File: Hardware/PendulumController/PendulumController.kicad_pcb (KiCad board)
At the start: 2 copper layers, 157 x 47 mm, 73 parts, among them J101 MOTOR, J102 ENCODER, J201 ICSP, J302 19V Input, J401 USBC, J402 PROG, Q101 MMBT3904, Q102 MMBT3906, SW201 RESET, SW202 START_SW, SW203 STOP/MODE_SW, U201 ATmega328P, U301 NCV1117ST50T3G, U401 FT232RL, Y201 16mHz

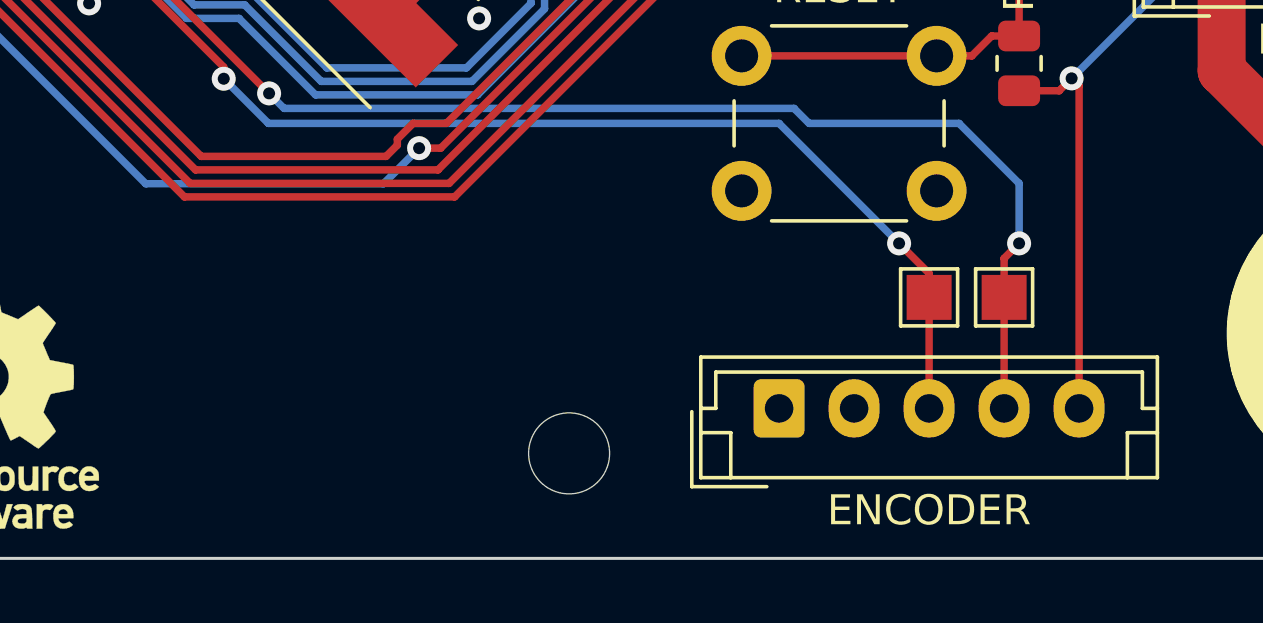
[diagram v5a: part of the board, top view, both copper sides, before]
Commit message: Add limit siwtch
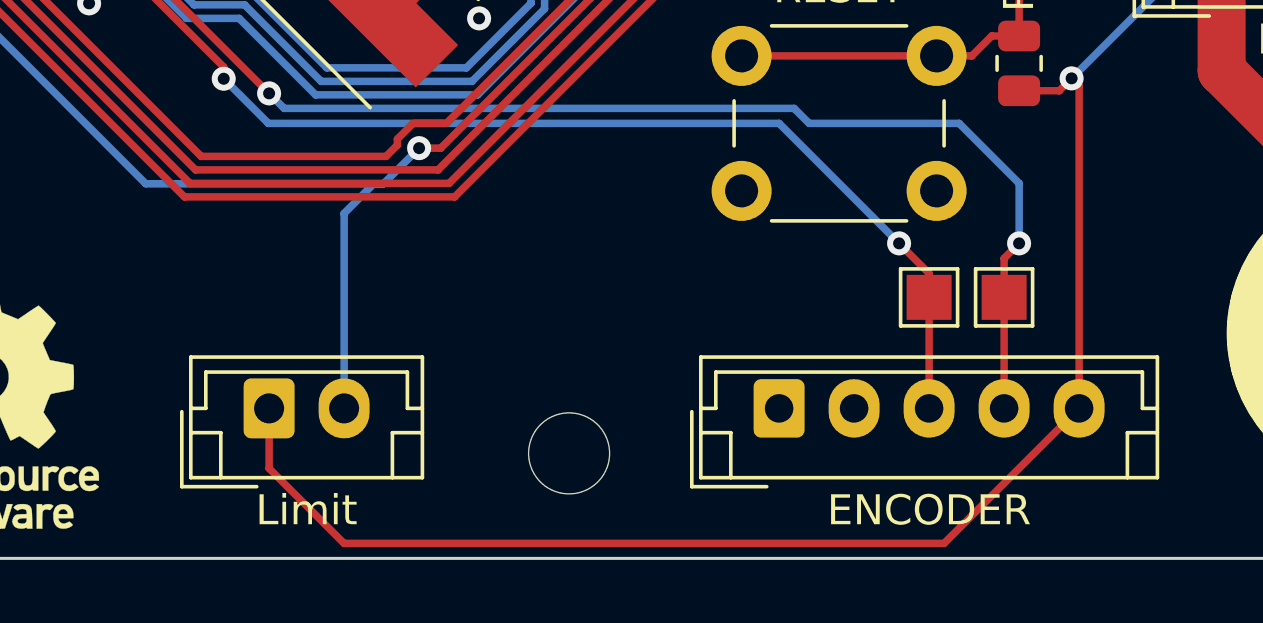
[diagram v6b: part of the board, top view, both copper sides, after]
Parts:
- added J202: Limit, Connector_JST:JST_EH_B2B-EH-A_1x02_P2.50mm_Vertical, F.Cu at (135.0, 108.5)
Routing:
- net +5V: track 297.9 -> 329.8 mm
- net /MCU/START: track 66.2 -> 74.4 mm
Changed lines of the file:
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@@
     (pad "" np_thru_hole circle (at 0 0) (size 2.7 2.7) (drill 2.7) (layers *.Cu *.Mask))
   )
+  (footprint "Connector_JST:JST_EH_B2B-EH-A_1x02_P2.50mm_Vertical" (layer "F.Cu")
+    (at 135 108.5)
+    (descr "JST EH series connector, B2B-EH-A (http://www.jst-mfg.com/product/pdf/eng/eEH.pdf), generated with kicad-footprint-generator")
+    (tags "connector JST EH vertical")
+    (property "Sheetfile" "mcu.kicad_sch")
+    (property "Sheetname" "MCU")
+    (attr through_hole)
+    (fp_text reference "J202" (at 1.25 -2.8) (layer "F.SilkS") hide
+      (effects (font (size 1 1) (thickness 0.15)))
+    )
+    (fp_text value "Limit" (at 1.25 3.4) (layer "F.SilkS")
+      (effects (font (size 1 1) (thickness 0.15)))
+    )
+    (fp_text user "${REFERENCE}" (at 1.25 1.5) (layer "F.Fab")
+      (effects (font (size 1 1) (thickness 0.15)))
+    )
+    (fp_line (start 4.61 -1.21) (end 4.61 0) (layer "F.SilkS") (width 0.12))
+    (fp_line (start 5.11 0.81) (end 4.11 0.81) (layer "F.SilkS") (width 0.12))
+    (fp_line (start 5.11 2.31) (end 5.11 -1.71) (layer "F.SilkS") (width 0.12))
+    (fp_line (start -2.91 0.11) (end -2.91 2.61) (layer "F.SilkS") (width 0.12))
+    (fp_line (start -2.11 -1.21) (end 4.61 -1.21) (layer "F.SilkS") (width 0.12))
+    (fp_line (start -1.61 0.81) (end -1.61 2.31) (layer "F.SilkS") (width 0.12))
+    (fp_line (start 5.11 -1.71) (end -2.61 -1.71) (layer "F.SilkS") (width 0.12))
+    (fp_line (start -2.91 2.61) (end -0.41 2.61) (layer "F.SilkS") (width 0.12))
+    (fp_line (start 4.11 0.81) (end 4.11 2.31) (layer "F.SilkS") (width 0.12))
+    (fp_line (start -2.61 0) (end -2.11 0) (layer "F.SilkS") (width 0.12))
+    (fp_line (start -2.61 0.81) (end -1.61 0.81) (layer "F.SilkS") (width 0.12))
+    (fp_line (start 4.61 0) (end 5.11 0) (layer "F.SilkS") (width 0.12))
+    (fp_line (start -2.11 0) (end -2.11 -1.21) (layer "F.SilkS") (width 0.12))
+    (fp_line (start -2.61 2.31) (end 5.11 2.31) (layer "F.SilkS") (width 0.12))
+    (fp_line (start -2.61 -1.71) (end -2.61 2.31) (layer "F.SilkS") (width 0.12))
+    (fp_line (start 5.5 -2.1) (end -3 -2.1) (layer "F.CrtYd") (width 0.05))
+    (fp_line (start -3 -2.1) (end -3 2.7) (layer "F.CrtYd") (width 0.05))
+    (fp_line (start -3 2.7) (end 5.5 2.7) (layer "F.CrtYd") (width 0.05))
+    (fp_line (start 5.5 2.7) (end 5.5 -2.1) (layer "F.CrtYd") (width 0.05))
+    (fp_line (start -2.5 -1.6) (end -2.5 2.2) (layer "F.Fab") (width 0.1))
+    (fp_line (start -2.5 2.2) (end 5 2.2) (layer "F.Fab") (width 0.1))
+    (fp_line (start -2.91 2.61) (end -0.41 2.61) (layer "F.Fab") (width 0.1))
+    (fp_line (start 5 -1.6) (end -2.5 -1.6) (layer "F.Fab") (width 0.1))
+    (fp_line (start -2.91 0.11) (end -2.91 2.61) (layer "F.Fab") (width 0.1))
+    (fp_line (start 5 2.2) (end 5 -1.6) (layer "F.Fab") (width 0.1))
+    (pad "1" thru_hole roundrect (at 0 0) (size 1.7 2) (drill 1) (layers *.Cu *.Mask) (roundrect_rratio 0.147059)
+      (net 3 "+5V") (pinfunction "Pin_1") (pintype "passive"))
+    (pad "2" thru_hole oval (at 2.5 0) (size 1.7 2) (drill 1) (layers *.Cu *.Mask)
+      (net 20 "/MCU/START") (pinfunction "Pin_2") (pintype "passive"))
+    (model "${KICAD6_3DMODEL_DIR}/Connector_JST.3dshapes/JST_EH_B2B-EH-A_1x02_P2.50mm_Vertical.wrl"
+      (offset (xyz 0 0 0))
+      (scale (xyz 1 1 1))
+      (rotate (xyz 0 0 0))
+    )
+  )
   (footprint "Capacitor_SMD:C_0805_2012Metric" (layer "F.Cu")
     (at 136.5 88 135)
@@
   (segment (start 148.749963 82.578464) (end 148.421536 82.578464) (width 0.55) (layer "F.Cu") (net 3))
   (segment (start 119.75 73.85) (end 119.75 75.25) (width 0.25) (layer "F.Cu") (net 3))
+  (segment (start 135 110.5) (end 135 108.5) (width 0.25) (layer "F.Cu") (net 3))
   (segment (start 190.5 69.3125) (end 193 69.3125) (width 1) (layer "F.Cu") (net 3))
   (segment (start 142.173869 88.023187) (end 141.523187 88.023187) (width 0.55) (layer "F.Cu") (net 3))
@@
   (segment (start 144 86.197056) (end 144 86) (width 0.55) (layer "F.Cu") (net 3))
   (segment (start 142.843324 87.353732) (end 144 86.197056) (width 0.55) (layer "F.Cu") (net 3))
+  (segment (start 162 108.5) (end 157.5 113) (width 0.25) (layer "F.Cu") (net 3))
   (segment (start 193.8125 69.3125) (end 196.25 71.75) (width 1) (layer "F.Cu") (net 3))
+  (segment (start 157.5 113) (end 137.5 113) (width 0.25) (layer "F.Cu") (net 3))
   (segment (start 196.25 71.75) (end 197.75 71.75) (width 1) (layer "F.Cu") (net 3))
   (segment (start 203.6 87.9) (end 204.3 87.2) (width 1) (layer "F.Cu") (net 3))
@@
   (segment (start 201.5 93) (end 201.5 90.5) (width 1) (layer "F.Cu") (net 3))
   (segment (start 161.5 84.75) (end 162.75 84.75) (width 0.25) (layer "F.Cu") (net 3))
+  (segment (start 137.5 113) (end 135 110.5) (width 0.25) (layer "F.Cu") (net 3))
   (segment (start 203.55 93.45) (end 201.95 93.45) (width 1) (layer "F.Cu") (net 3))
   (segment (start 207.475 74.925) (end 206.55 74) (width 0.45) (layer "F.Cu") (net 3))
@@
   (segment (start 107.0875 81.75) (end 106.3375 82.5) (width 0.25) (layer "B.Cu") (net 20))
   (segment (start 115.974733 86.098831) (end 130.888201 101.012299) (width 0.25) (layer "B.Cu") (net 20))
+  (segment (start 138.487701 101.012299) (end 137.5 102) (width 0.25) (layer "B.Cu") (net 20))
   (segment (start 138.813201 101.012299) (end 140 99.8255) (width 0.25) (layer "B.Cu") (net 20))
   (segment (start 110.4125 81.75) (end 107.0875 81.75) (width 0.25) (layer "B.Cu") (net 20))
   (segment (start 105.5875 81.75) (end 106.3375 82.5) (width 0.25) (layer "B.Cu") (net 20))
+  (segment (start 138.813201 101.012299) (end 138.487701 101.012299) (width 0.25) (layer "B.Cu") (net 20))
+  (segment (start 137.5 102) (end 137.5 108.5) (width 0.25) (layer "B.Cu") (net 20))
   (segment (start 140.90901 99) (end 148.863604 91.045406) (width 0.25) (layer "F.Cu") (net 21))
   (segment (start 97 84) (end 94.75 81.75) (width 0.25) (layer "F.Cu") (net 21))

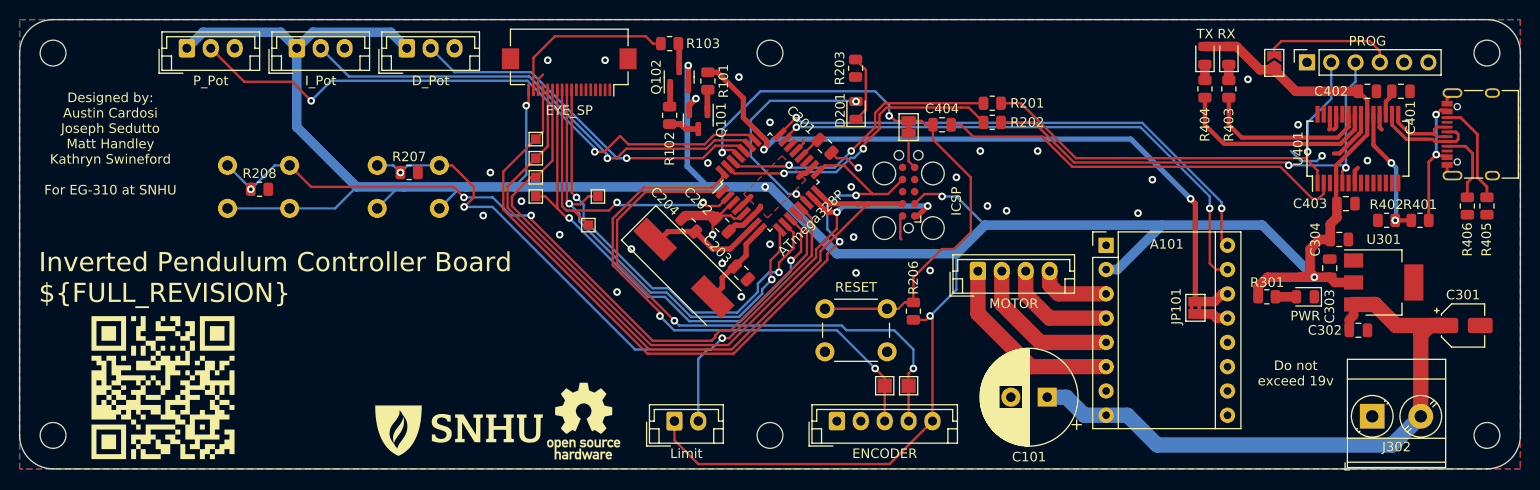
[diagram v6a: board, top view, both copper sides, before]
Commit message: Add usb terminators
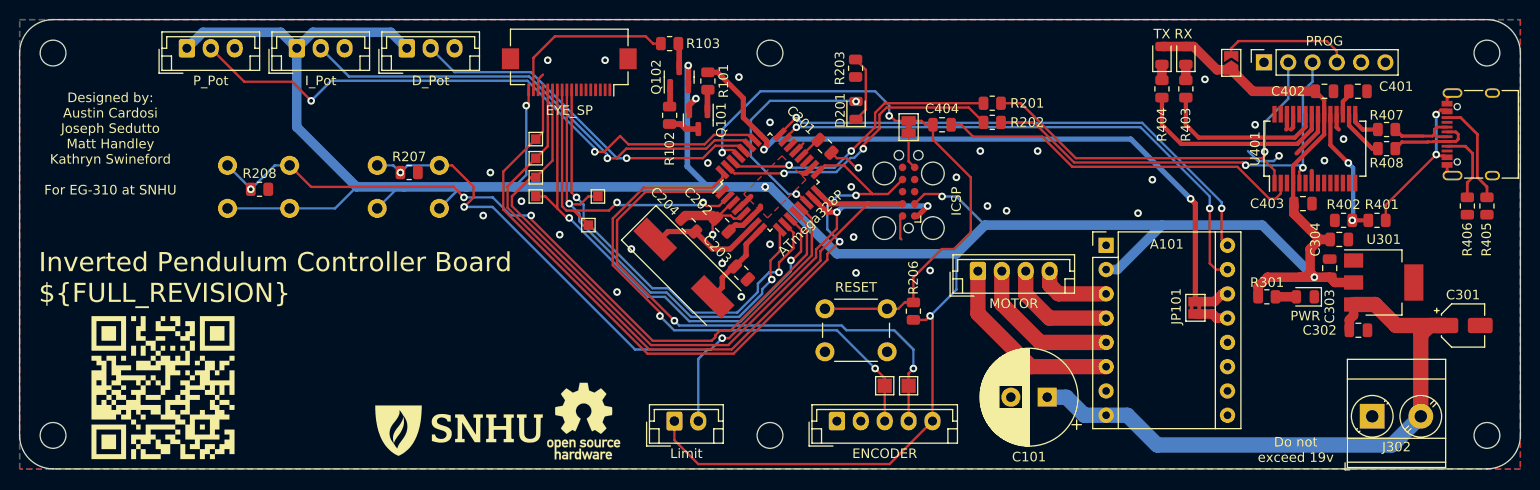
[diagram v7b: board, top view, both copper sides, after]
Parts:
- added R407: 22R, Resistor_SMD:R_0805_2012Metric, F.Cu at (209.5, 78.0)
- added R408: 22R, Resistor_SMD:R_0805_2012Metric, F.Cu at (209.5, 80.0)
- moved C401 4.50 mm to (206.5, 74.0)
- moved C402 4.50 mm to (203.0, 74.0)
- moved C403 4.50 mm to (200.8, 85.8)
- moved D401 4.50 mm to (188.5, 70.2)
- moved D402 4.50 mm to (186.0, 70.2)
- moved J402 4.50 mm to (196.7, 71.0)
- moved JP401 4.50 mm to (193.2, 71.0)
- moved R401 4.50 mm to (208.5, 87.5)
- moved R402 4.50 mm to (205.0, 87.5)
- moved R403 4.50 mm to (188.5, 73.8)
- moved R404 4.50 mm to (186.0, 73.8)
- moved U401 4.50 mm to (202.0, 80.0)
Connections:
- U401 pad 15: /Programming/USB+ -> Net-(U401-Pad15)
- U401 pad 16: /Programming/USB- -> Net-(U401-Pad16)
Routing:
- net Net-(U401-Pad16): track 0.00 -> 5.21 mm
- net Net-(C404-Pad2): track 43.5 -> 39.0 mm
- net /MCU/RXD: track 48.5 -> 44.0 mm
- net /MCU/TXD: track 51.3 -> 46.8 mm
- net Net-(U401-Pad15): track 0.00 -> 3.52 mm
- net /Programming/USB-: track 10.6 -> 8.78 mm
- net VBUS: track 13.6 -> 15.4 mm
- net GND: track 41.3 -> 39.8 mm, vias 32 -> 33
- net /Programming/USB+: track 8.53 -> 7.81 mm

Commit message: Silkscreen!
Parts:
- added G***: LOGO, Misc:JLCPCB, F.Cu at (124.0, 102.0)
- added G***: LOGO, KenwoodFox:KITSUNE_LOGO, B.Cu at (79.0, 107.5)
- added REF**: KiCad-Logo2_8mm_SilkScreen, Symbol:KiCad-Logo2_8mm_SilkScreen, F.Cu at (102.5, 99.5)
- moved REF** 38.7 mm to (87.5, 101.0)
- moved SNHU_NEW*** 24.8 mm to (94.0, 93.0)
- moved QRCODE 9.22 mm to (75.5, 98.0)
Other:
- board text added: "Built and Prototyped by Kitsune Scientific"
